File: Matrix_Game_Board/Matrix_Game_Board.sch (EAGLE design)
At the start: 48 parts, among them J1 AVR_SPI_PRG_6NS, J2 AVR_SPI_PRG_6NS, J3 AVR_SPI_PRG_6NS, J4 AVR_SPI_PRG_6NS

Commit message: Added start and select buttons to matrix board and moved accelerometer to the middle of the board
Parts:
- added C10, C11, C8, C9: (no value), resistor:C-USC0603
- added U$24, U$26: SMDTACTILE, ScottSilver:SMDTACTILE
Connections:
- new net SELECT: PI-HEADER.15, U$26.P$1
- new net START: PI-HEADER.13, U$24.P$1
- net A: now also PI-HEADER.7; no longer PI-HEADER.16
- net B: now also PI-HEADER.11; no longer PI-HEADER.12
- net DOWN: now also PI-HEADER.18; no longer PI-HEADER.13
- net GND: now also C10.2, C11.2, C8.2, C9.2, U$24.P$4, U$26.P$4
- net LEFT: now also PI-HEADER.16; no longer PI-HEADER.15
- net RESET: no longer PI-HEADER.22
- net RIGHT: now also PI-HEADER.12; no longer PI-HEADER.18
- net UP: now also PI-HEADER.22; no longer PI-HEADER.7
- net VCC: now also C10.1, C11.1, C8.1, C9.1
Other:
- moved on the sheet: PI-HEADER

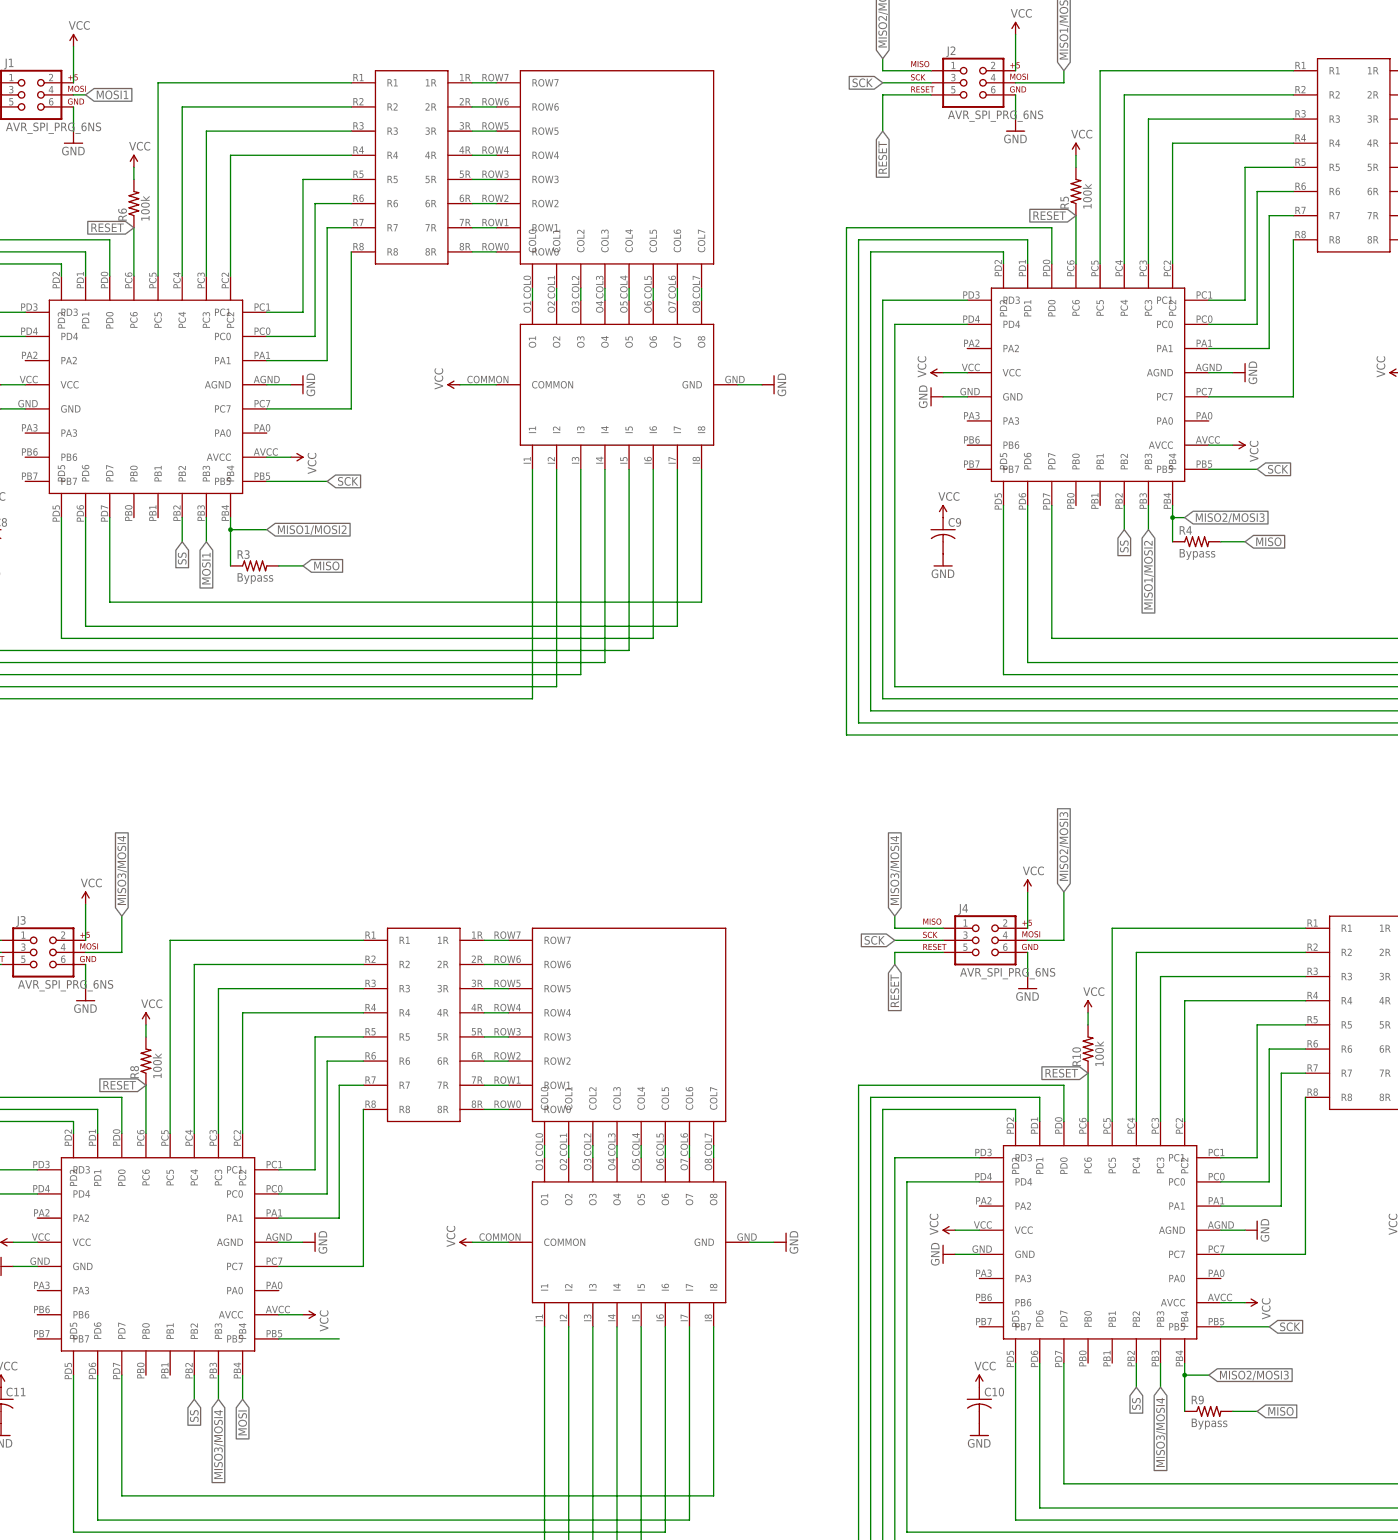
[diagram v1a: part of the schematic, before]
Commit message: Corrected some net names on Gamer PCB
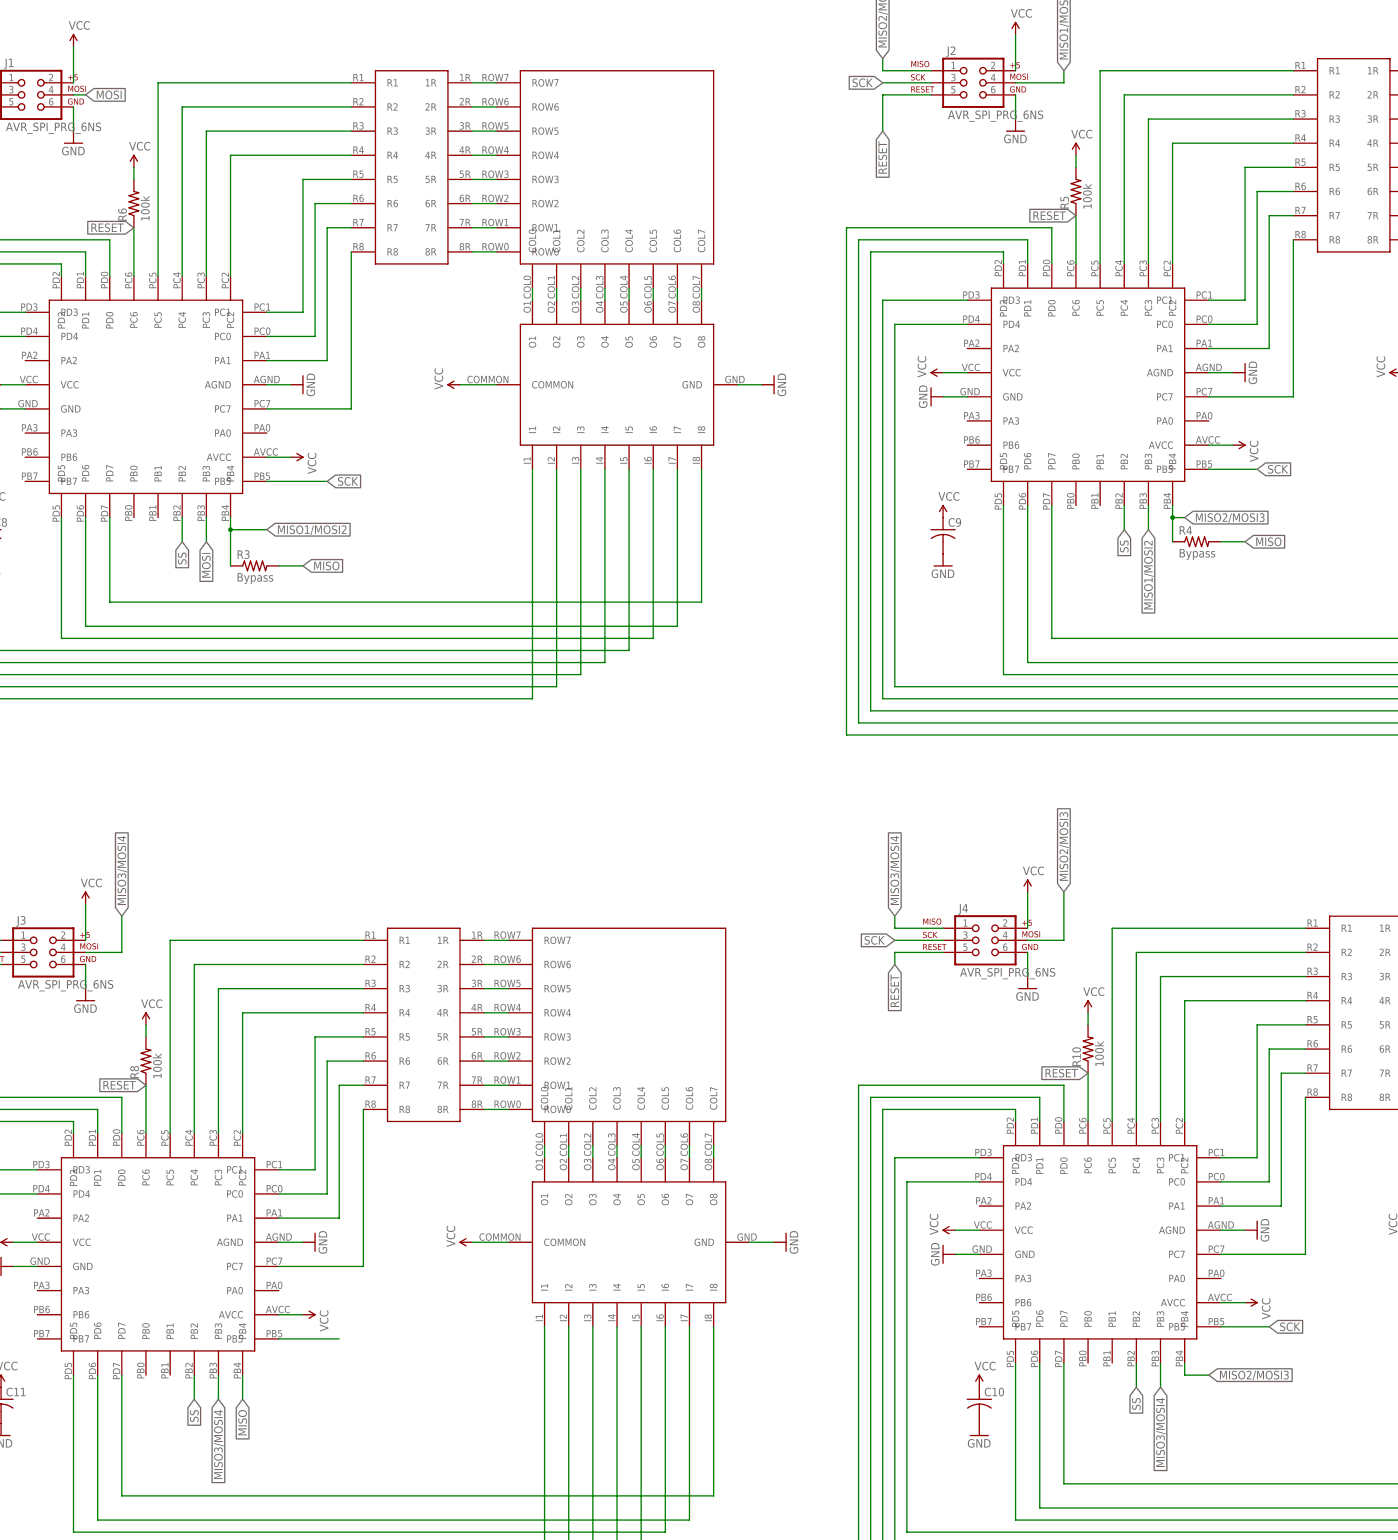
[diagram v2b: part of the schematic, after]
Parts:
- removed R9: Bypass, resistor:R-US_R0805
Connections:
- removed net MOSI1: J1.4, U$9.PB3
- net MISO: now also U$11.PB4; no longer R9.2
- net MISO2/MOSI3: no longer R9.1
- net MOSI: now also J1.4, U$9.PB3; no longer U$11.PB4
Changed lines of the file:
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@@
 <part name="GND16" library="SparkFun-Aesthetics" deviceset="GND" device=""/>
 <part name="SUPPLY24" library="SparkFun-Aesthetics" deviceset="VCC" device=""/>
-<part name="R9" library="resistor" deviceset="R-US_" device="R0805" value="Bypass"/>
 <part name="R10" library="resistor" deviceset="R-US_" device="R0805" value="100k"/>
 <part name="SUPPLY25" library="SparkFun-Aesthetics" deviceset="VCC" device=""/>
@@
 <instance part="GND16" gate="1" x="269.24" y="182.88"/>
 <instance part="SUPPLY24" gate="G$1" x="269.24" y="203.2"/>
-<instance part="R9" gate="G$1" x="307.34" y="93.98"/>
 <instance part="R10" gate="G$1" x="281.94" y="170.18" rot="R90"/>
 <instance part="SUPPLY25" gate="G$1" x="281.94" y="177.8"/>
@@
 </segment>
 </net>
-<net name="MOSI" class="0">
-<segment>
-<wire x1="426.72" y1="-7.62" x2="444.5" y2="-7.62" width="0.1524" layer="91"/>
-<label x="444.5" y="-7.62" size="1.016" layer="95" rot="MR180" xref="yes"/>
-<pinref part="PI-HEADER" gate="A" pin="19"/>
-</segment>
-<segment>
-<pinref part="U$11" gate="G$1" pin="PB4"/>
-<wire x1="104.14" y1="96.52" x2="104.14" y2="101.6" width="0.1524" layer="91"/>
-<label x="104.14" y="96.52" size="1.778" layer="95" rot="R270" xref="yes"/>
-</segment>
-</net>
 <net name="MISO" class="0">
 <segment>
@@
 <wire x1="309.88" y1="276.86" x2="314.96" y2="276.86" width="0.1524" layer="91"/>
 <label x="314.96" y="276.86" size="1.778" layer="95" xref="yes"/>
-</segment>
-<segment>
-<pinref part="R9" gate="G$1" pin="2"/>
-<wire x1="312.42" y1="93.98" x2="317.5" y2="93.98" width="0.1524" layer="91"/>
-<label x="317.5" y="93.98" size="1.778" layer="95" xref="yes"/>
 </segment>
 <segment>
@@
 <wire x1="45.72" y1="193.04" x2="45.72" y2="195.58" width="0.1524" layer="91"/>
 <label x="45.72" y="195.58" size="1.778" layer="95" rot="R90" xref="yes"/>
+</segment>
+<segment>
+<pinref part="U$11" gate="G$1" pin="PB4"/>
+<wire x1="104.14" y1="96.52" x2="104.14" y2="101.6" width="0.1524" layer="91"/>
+<label x="104.14" y="96.52" size="1.778" layer="95" rot="R270" xref="yes"/>
 </segment>
 </net>
@@
 </segment>
 </net>
-<net name="MOSI1" class="0">
-<segment>
-<pinref part="J1" gate="G$1" pin="4"/>
-<wire x1="68.58" y1="370.84" x2="71.12" y2="370.84" width="0.1524" layer="91"/>
-<label x="71.12" y="370.84" size="1.778" layer="95" xref="yes"/>
-</segment>
-<segment>
-<pinref part="U$9" gate="G$1" pin="PB3"/>
-<wire x1="96.52" y1="281.94" x2="96.52" y2="276.86" width="0.1524" layer="91"/>
-<label x="96.52" y="276.86" size="1.778" layer="95" rot="R270" xref="yes"/>
-</segment>
-</net>
 <net name="MISO1/MOSI2" class="0">
 <segment>
@@
 <segment>
 <pinref part="U$15" gate="G$1" pin="PB4"/>
-<wire x1="302.26" y1="93.98" x2="302.26" y2="101.6" width="0.1524" layer="91"/>
-<pinref part="R9" gate="G$1" pin="1"/>
 <wire x1="302.26" y1="101.6" x2="302.26" y2="104.14" width="0.1524" layer="91"/>
 <wire x1="302.26" y1="101.6" x2="307.34" y2="101.6" width="0.1524" layer="91"/>
-<junction x="302.26" y="101.6"/>
 <label x="307.34" y="101.6" size="1.778" layer="95" xref="yes"/>
 </segment>
@@
 </segment>
 </net>
+<net name="MOSI" class="0">
+<segment>
+<wire x1="426.72" y1="-7.62" x2="444.5" y2="-7.62" width="0.1524" layer="91"/>
+<label x="444.5" y="-7.62" size="1.016" layer="95" rot="MR180" xref="yes"/>
+<pinref part="PI-HEADER" gate="A" pin="19"/>
+</segment>
+<segment>
+<pinref part="J1" gate="G$1" pin="4"/>
+<wire x1="68.58" y1="370.84" x2="71.12" y2="370.84" width="0.1524" layer="91"/>
+<label x="71.12" y="370.84" size="1.778" layer="95" xref="yes"/>
+</segment>
+<segment>
+<pinref part="U$9" gate="G$1" pin="PB3"/>
+<wire x1="96.52" y1="281.94" x2="96.52" y2="276.86" width="0.1524" layer="91"/>
+<label x="96.52" y="276.86" size="1.778" layer="95" rot="R270" xref="yes"/>
+</segment>
+</net>

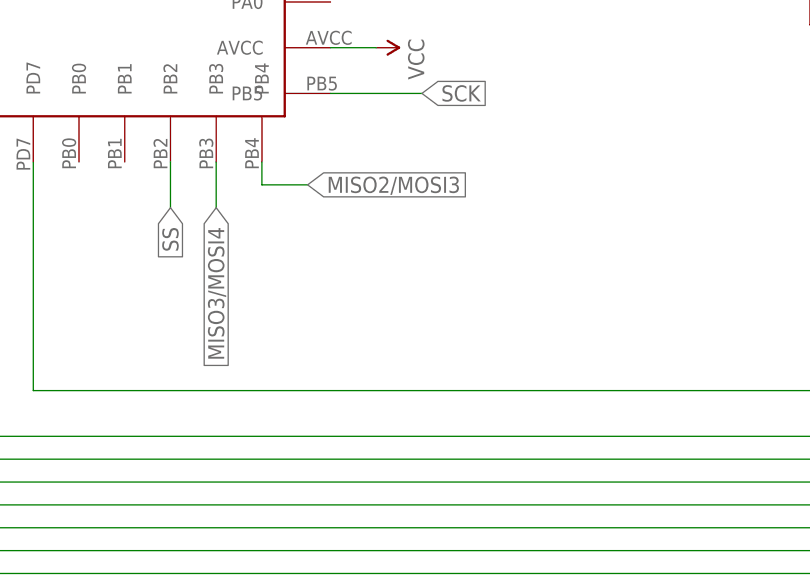
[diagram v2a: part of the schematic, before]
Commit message: Corrected some more net names on Gamer PCB
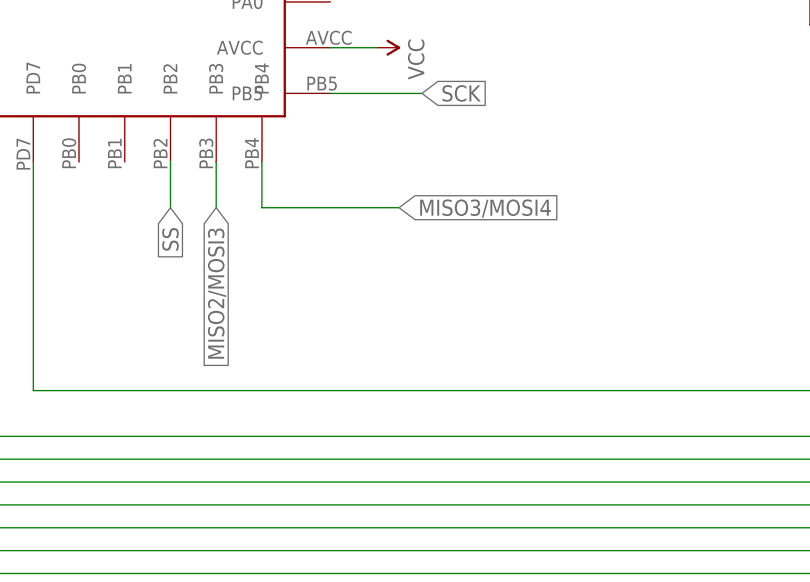
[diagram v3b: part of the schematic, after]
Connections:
- net MISO2/MOSI3: now also U$15.PB3; no longer U$15.PB4
- net MISO3/MOSI4: now also U$15.PB4; no longer U$15.PB3
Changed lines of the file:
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@@
 </segment>
 <segment>
-<pinref part="U$15" gate="G$1" pin="PB4"/>
-<wire x1="302.26" y1="101.6" x2="302.26" y2="104.14" width="0.1524" layer="91"/>
-<wire x1="302.26" y1="101.6" x2="307.34" y2="101.6" width="0.1524" layer="91"/>
-<label x="307.34" y="101.6" size="1.778" layer="95" xref="yes"/>
+<pinref part="U$15" gate="G$1" pin="PB3"/>
+<wire x1="297.18" y1="104.14" x2="297.18" y2="99.06" width="0.1524" layer="91"/>
+<label x="297.18" y="99.06" size="1.778" layer="95" rot="R270" xref="yes"/>
 </segment>
 </net>
@@
 </segment>
 <segment>
-<pinref part="U$15" gate="G$1" pin="PB3"/>
-<wire x1="297.18" y1="104.14" x2="297.18" y2="99.06" width="0.1524" layer="91"/>
-<label x="297.18" y="99.06" size="1.778" layer="95" rot="R270" xref="yes"/>
+<pinref part="U$15" gate="G$1" pin="PB4"/>
+<wire x1="302.26" y1="104.14" x2="302.26" y2="99.06" width="0.1524" layer="91"/>
+<wire x1="302.26" y1="99.06" x2="317.5" y2="99.06" width="0.1524" layer="91"/>
+<label x="317.5" y="99.06" size="1.778" layer="95" xref="yes"/>
 </segment>
 </net>
